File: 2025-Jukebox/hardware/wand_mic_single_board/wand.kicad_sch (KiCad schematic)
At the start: 52 parts, among them J1 USB_C_Receptacle_USB2.0, J4 Conn_01x02, J9 Conn_01x02, Q1 MUN5214DW1T1G, Q3 CJ3139K, SW1 SW_Push, U1 CP2104, U2 ESP32-PICO-D4, U3 ICM-20948, U4 TP4065-4.2V, U5 TLV76718DRVx, U6 LY68L6400SLIT, U7 PCA9306, U9 TLV76733DRVx

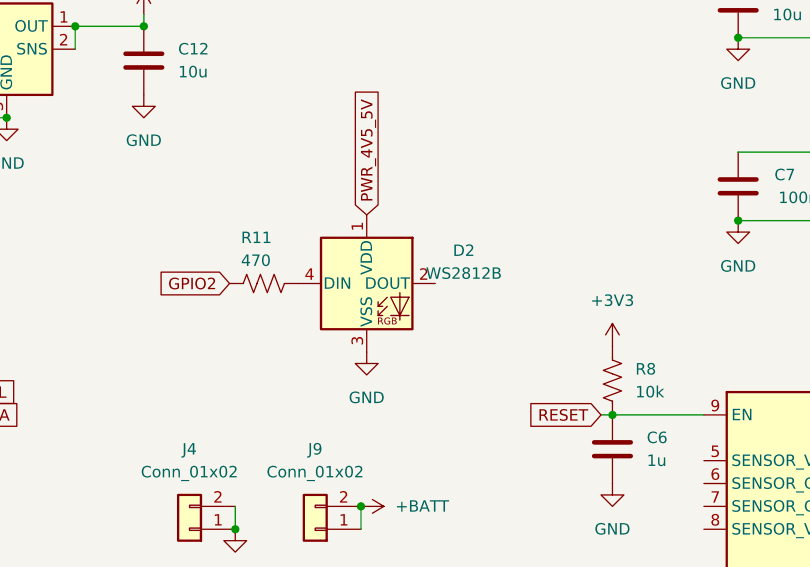
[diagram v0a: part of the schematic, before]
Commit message: Added footprint for light pipe
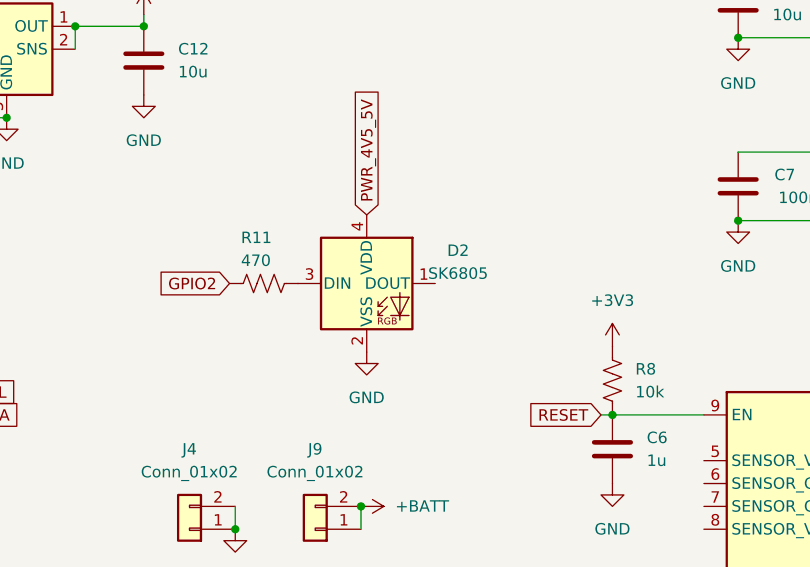
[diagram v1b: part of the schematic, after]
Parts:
- removed D2: WS2812B, LED_SMD:LED_WS2812B_PLCC4_5.0x5.0mm_P3.2mm, symbol LED:WS2812B
- added D2: SK6805, LED_SMD:LED_SK6805_PLCC4_2.4x2.7mm_P1.3mm, symbol LED:SK6805
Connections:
- net GND: now also D2.2 (VSS)
- net PWR_4V5_5V: now also D2.4 (VDD)
- net at R11.1: now also D2.3 (DIN)
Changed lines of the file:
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@@
-    )
-  )
-  (symbol (lib_id "LED:WS2812B") (at 182.245 64.135 0) (unit 1)
-    (in_bom yes) (on_board yes) (dnp no) (fields_autoplaced)
-    (property "Reference" "D2" (at 193.04 60.4871 0)
-      (effects (font (size 1.27 1.27)))
-    )
-    (property "Value" "WS2812B" (at 193.04 63.0271 0)
-      (effects (font (size 1.27 1.27)))
-    )
-    (property "Footprint" "LED_SMD:LED_WS2812B_PLCC4_5.0x5.0mm_P3.2mm" (at 183.515 71.755 0)
-      (effects (font (size 1.27 1.27)) (justify left top) hide)
-    )
-    (property "Datasheet" "https://cdn-shop.adafruit.com/datasheets/WS2812B.pdf" (at 184.785 73.66 0)
-      (effects (font (size 1.27 1.27)) (justify left top) hide)
-    )
-    (pin "1")
-    (pin "2")
-    (pin "3")
-    (pin "4")
-    (instances
-      (project "wand"
-        (path "/57fbe485-87aa-4709-9ba0-ed0723b6c939"
-          (reference "D2") (unit 1)
-        )
-      )
     )
   )
@@
         )
       )
+    )
+  )
+  (symbol (lib_id "LED:SK6805") (at 182.245 64.135 0) (unit 1)
+    (in_bom yes) (on_board yes) (dnp no) (fields_autoplaced)
+    (property "Reference" "D2" (at 192.405 60.4871 0)
+      (effects (font (size 1.27 1.27)))
+    )
+    (property "Value" "SK6805" (at 192.405 63.0271 0)
+      (effects (font (size 1.27 1.27)))
+    )
+    (property "Footprint" "LED_SMD:LED_SK6805_PLCC4_2.4x2.7mm_P1.3mm" (at 183.515 71.755 0)
+      (effects (font (size 1.27 1.27)) (justify left top) hide)
+    )
+    (property "Datasheet" "https://cdn-shop.adafruit.com/product-files/3484/3484_Datasheet.pdf" (at 184.785 73.66 0)
+      (effects (font (size 1.27 1.27)) (justify left top) hide)
+    )
+    (pin "1")
+    (pin "2")
+    (pin "3")
+    (pin "4")
+    (instances
+      (project "wand"
+        (path "/57fbe485-87aa-4709-9ba0-ed0723b6c939"
+          (reference "D2") (unit 1)
+        )
+      )

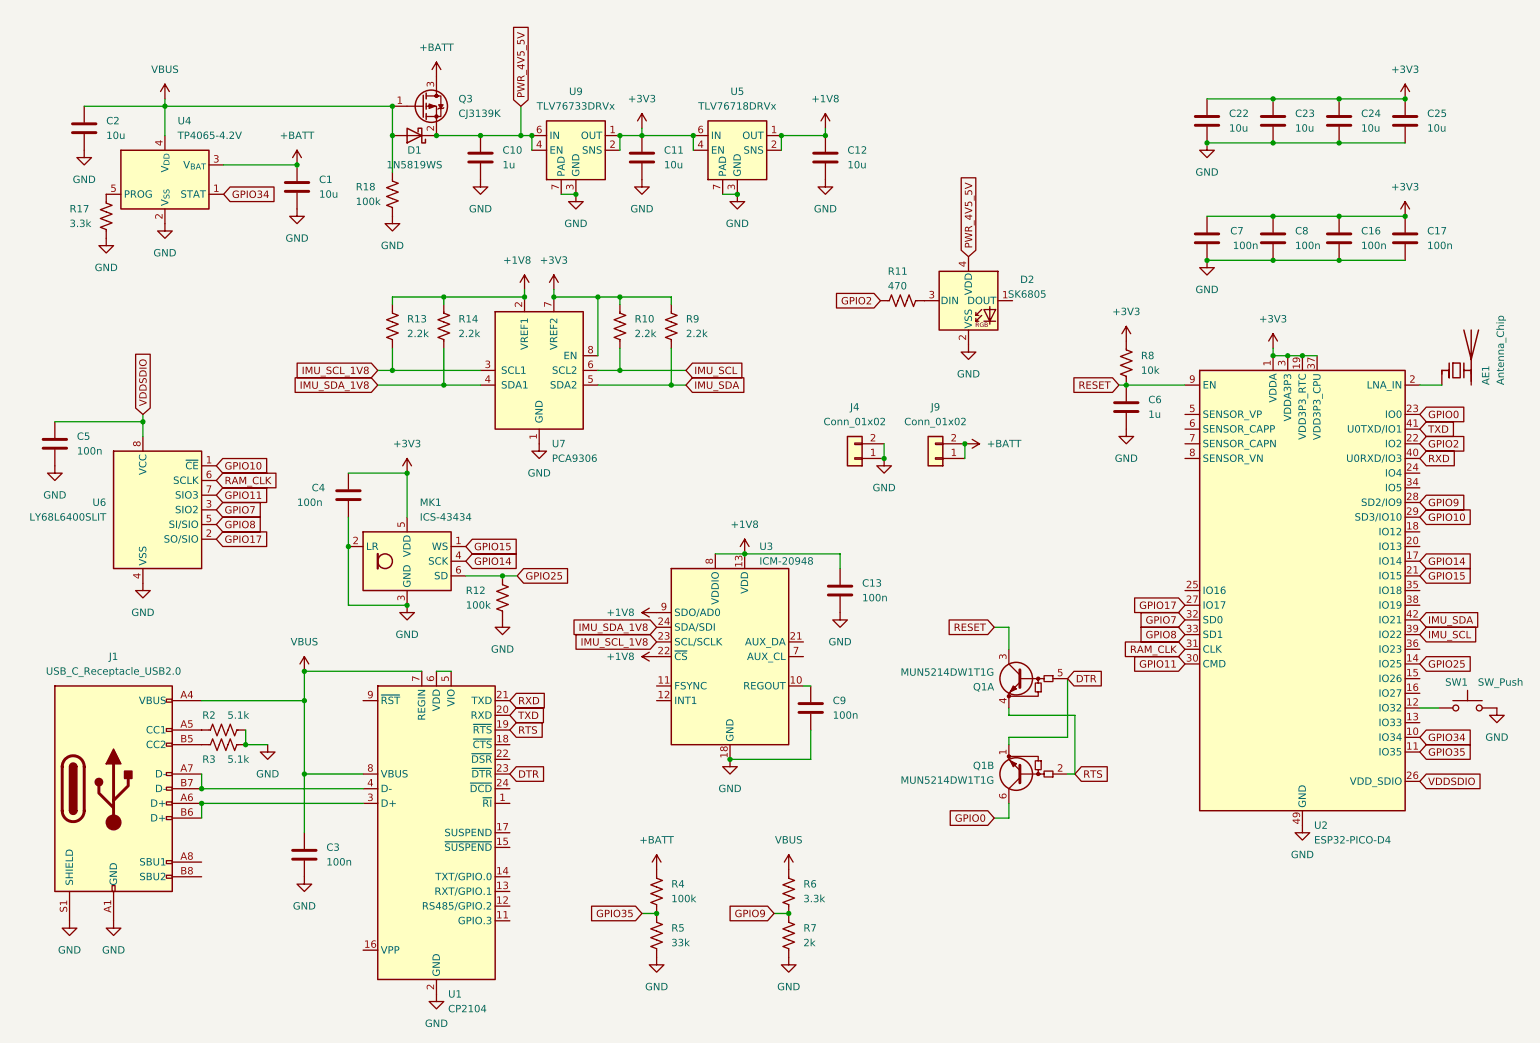
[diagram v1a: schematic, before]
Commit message: Replaced IMU with BNO055
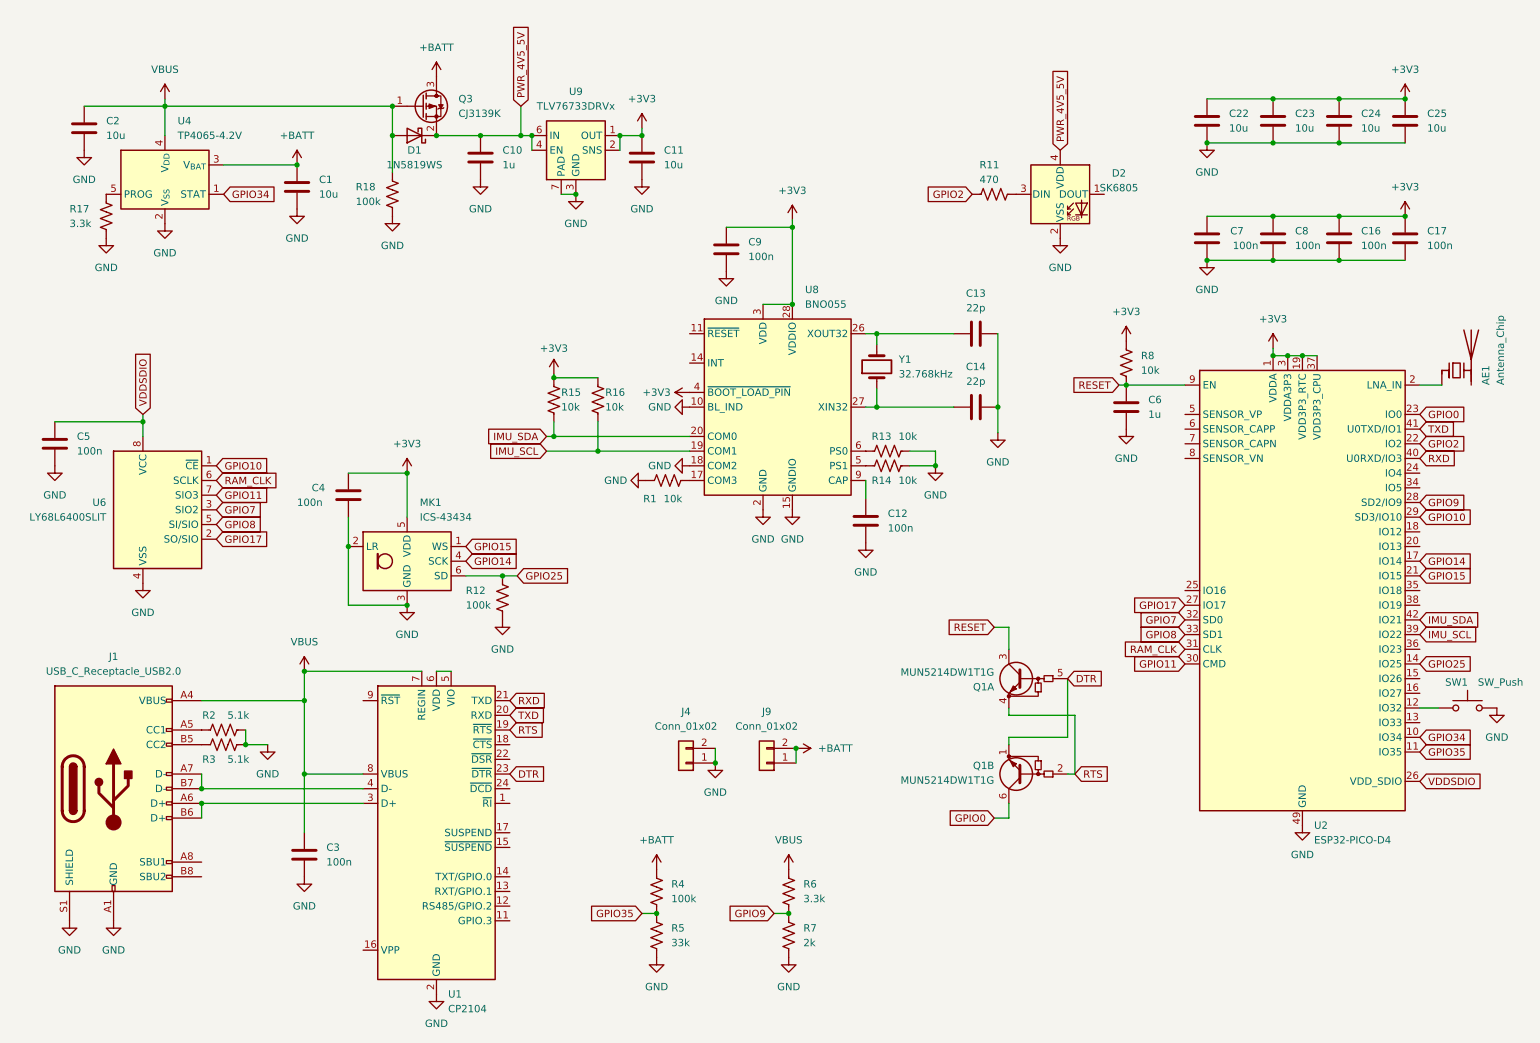
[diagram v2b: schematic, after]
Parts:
- removed R10, R9: 2.2k, Resistor_SMD:R_0402_1005Metric, symbol Device:R_US
- removed U3: ICM-20948, Sensor_Motion:InvenSense_QFN-24_3x3mm_P0.4mm, symbol Sensor_Motion:ICM-20948
- removed U5: TLV76718DRVx, Package_SON:WSON-6-1EP_2x2mm_P0.65mm_EP1x1.6mm_ThermalVias, symbol Regulator_Linear:TLV76718DRVx
- removed U7: PCA9306, Package_SO:VSSOP-8_2.3x2mm_P0.5mm, symbol Interface:PCA9306
- added C14: 22p, Capacitor_SMD:C_0402_1005Metric, symbol Device:C
- added R1, R15, R16: 10k, Resistor_SMD:R_0402_1005Metric, symbol Device:R_US
- added U8: BNO055, Package_LGA:LGA-28_5.2x3.8mm_P0.5mm, symbol Sensor_Motion:BNO055
- added Y1: 32.768kHz, Crystal:Crystal_SMD_3215-2Pin_3.2x1.5mm, symbol Device:Crystal
- C12: value 10u -> 100n
- C13: value 100n -> 22p
- C9: footprint Capacitor_SMD:C_0603_1608Metric -> Capacitor_SMD:C_0402_1005Metric
- R13, R14: value 2.2k -> 10k
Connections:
- net +3V3: now also C9.1, R15.1, R16.1, U8.28 (VDDIO), U8.3 (VDD), U8.4 (~{BOOT_LOAD_PIN})
- net GND: now also R13.1, R14.1, C14.2, R1.2, U8.10 (BL_IND), U8.15 (GNDIO), U8.16 (GNDIO), U8.18 (COM2), U8.2 (GND), U8.25 (GNDIO)
- net IMU_SCL: now also R16.2, U8.19 (COM1)
- net IMU_SDA: now also R15.2, U8.20 (COM0)
- removed net +1V8: C12.1, C13.1, R13.1, R14.1
- net IMU_SCL_1V8: no longer names the net of R13.2
- net IMU_SCL_1V8: now also U8.6 (PS0)
- net IMU_SDA_1V8: no longer names the net of R14.2
- net IMU_SDA_1V8: now also U8.5 (PS1)
- new net: R1.1, U8.17 (COM3)
- new net: C13.1, U8.26 (XOUT32), Y1.2
- new net: C14.1, U8.27 (XIN32), Y1.1
- new net: C12.1, U8.9 (CAP)
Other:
- moved on the sheet: D2, J4, J9, R11

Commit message: Changed button location
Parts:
- SW1: footprint Button_Switch_THT:SW_PUSH_6mm -> Button_Switch_THT:SW_PUSH_6mm_H13mm
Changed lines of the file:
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@@
       (effects (font (size 1.27 1.27)))
     )
-    (property "Footprint" "Button_Switch_THT:SW_PUSH_6mm" (at 268.605 129.54 0)
+    (property "Footprint" "Button_Switch_THT:SW_PUSH_6mm_H13mm" (at 268.605 129.54 0)
       (effects (font (size 1.27 1.27)) hide)
     )
